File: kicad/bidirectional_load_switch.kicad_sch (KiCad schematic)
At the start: 10 parts, among them U1 SISS94DN-T1-GE3, U2 RTBS60M, U3 UCC23313DWYR, U4 DMN65D8L-7

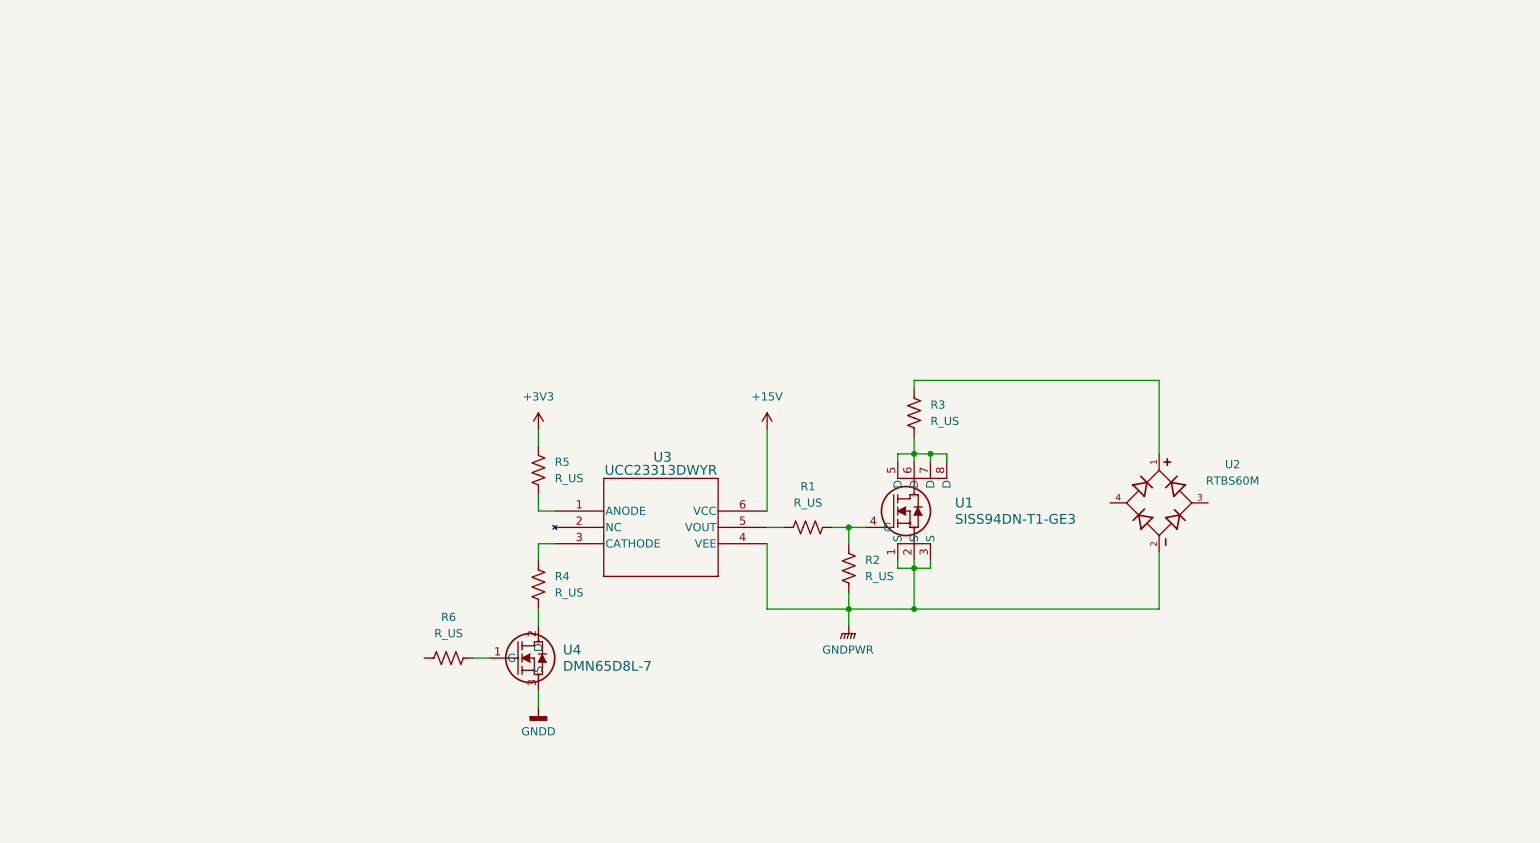
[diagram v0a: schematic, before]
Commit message: implementing switch design
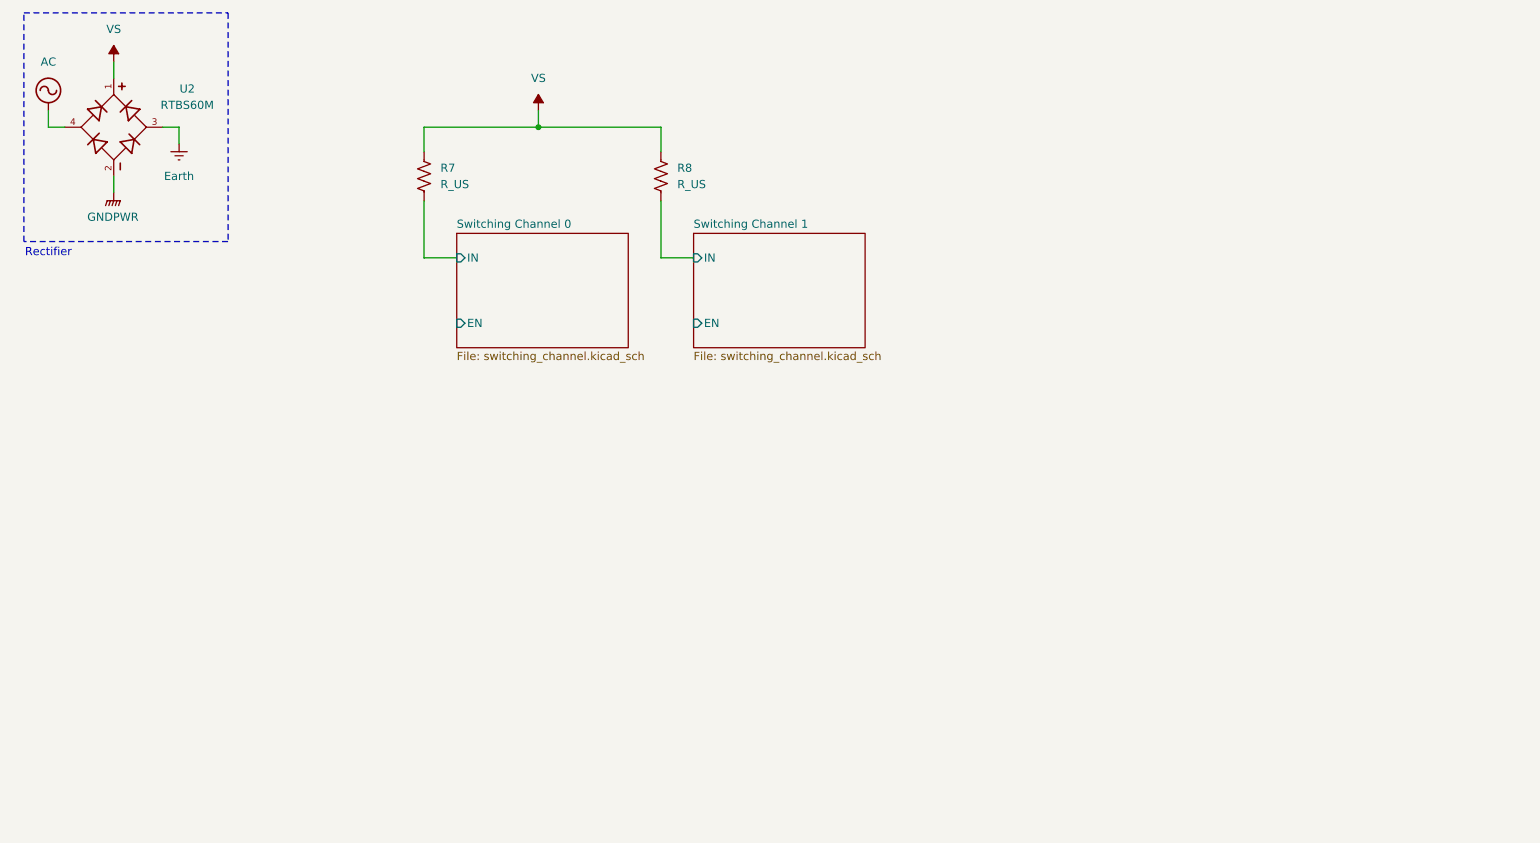
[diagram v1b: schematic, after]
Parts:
- removed R1, R2, R3, R4, R5, R6: R_US, Resistor_SMD:R_2512_6332Metric_Pad1.40x3.35mm_HandSolder, symbol Device:R_US
- removed U1: SISS94DN-T1-GE3, Big Mosfet:MOSFET_3DN-T1-GE3_VIS, symbol Mosfet:SISS94DN-T1-GE3
- removed U3: UCC23313DWYR, Gate Driver:SOIC6_DWY_TEX, symbol Gate Driver:UCC23313DWYR
- removed U4: DMN65D8L-7, Small Mosfet:SOT-23_2P9X1P3_DIO, symbol Small Mosfet:DMN65D8L-7
- added R7, R8: R_US, symbol Device:R_US
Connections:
- net VS: now reaches U2.1
- net VS: now also R7.1, R8.1
- net Earth: now reaches U2.3
- net AC: now reaches U2.4
- new net Switching Channel 0/IN: R7.2
- new net Switching Channel 1/IN: R8.2
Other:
- added sheet Switching Channel 0 (switching_channel.kicad_sch)
- added sheet Switching Channel 1 (switching_channel.kicad_sch)
- note added: "Rectifier"
- company: (none) -> University of Wisconsin-Platteville
- title: (none) -> Bidirectional Load Switch

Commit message: kicad
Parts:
- removed R7, R8: R_US, symbol Device:R_US
- added R25, R26, R27, R28, R29, R30, R31, R32: R_US, symbol Device:R_US
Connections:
- net Channel 0/IN: now also R25.2
- new net: R25.1, R26.1, R27.1, R28.1, R29.1, R30.1, R31.1, R32.1
- new net Channel 1/IN: R26.2
- new net Channel 2/IN: R27.2
- new net Channel 3/IN: R28.2
- new net Channel 4/IN: R29.2
- new net Channel 5/IN: R30.2
- new net Channel 6/IN: R31.2
- new net Channel 7/IN: R32.2
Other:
- sheet Switching Channel 0 renamed Channel 0
- removed sheet Switching Channel 1
- added sheet Channel 1 (switching_channel.kicad_sch)
- added sheet Channel 2 (switching_channel.kicad_sch)
- added sheet Channel 3 (switching_channel.kicad_sch)
- added sheet Channel 4 (switching_channel.kicad_sch)
- added sheet Channel 5 (switching_channel.kicad_sch)
- added sheet Channel 6 (switching_channel.kicad_sch)
- added sheet Channel 7 (switching_channel.kicad_sch)

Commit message: kicad
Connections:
- net VS: now also R25.1, R26.1, R27.1, R28.1, R29.1, R30.1, R31.1, R32.1
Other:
- moved on the sheet: R25, R26, R27, R28, R29, R30, R31, R32, U2

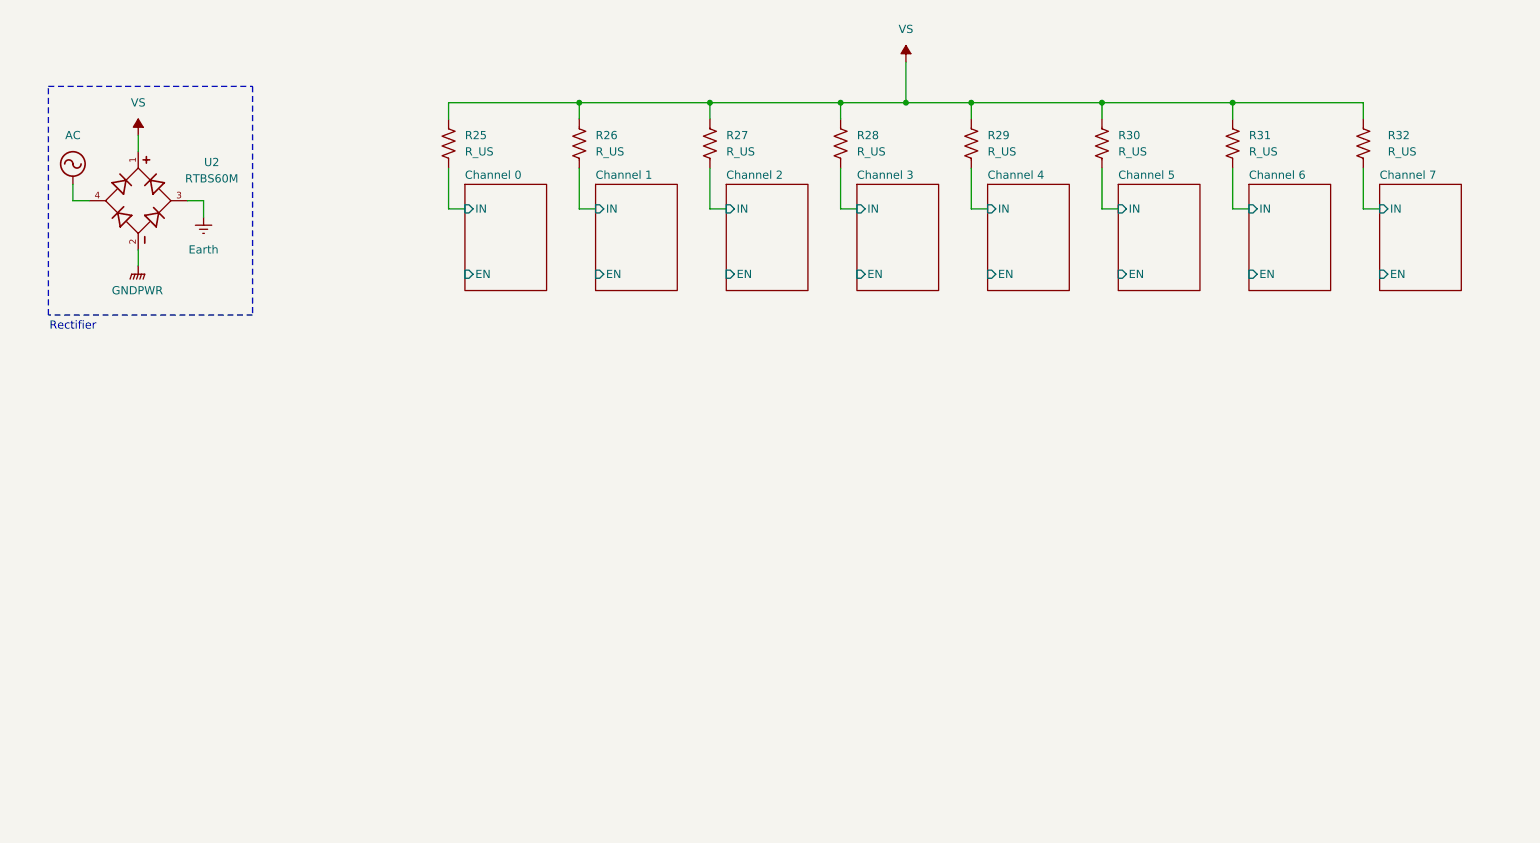
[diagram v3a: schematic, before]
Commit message: updated switch topology
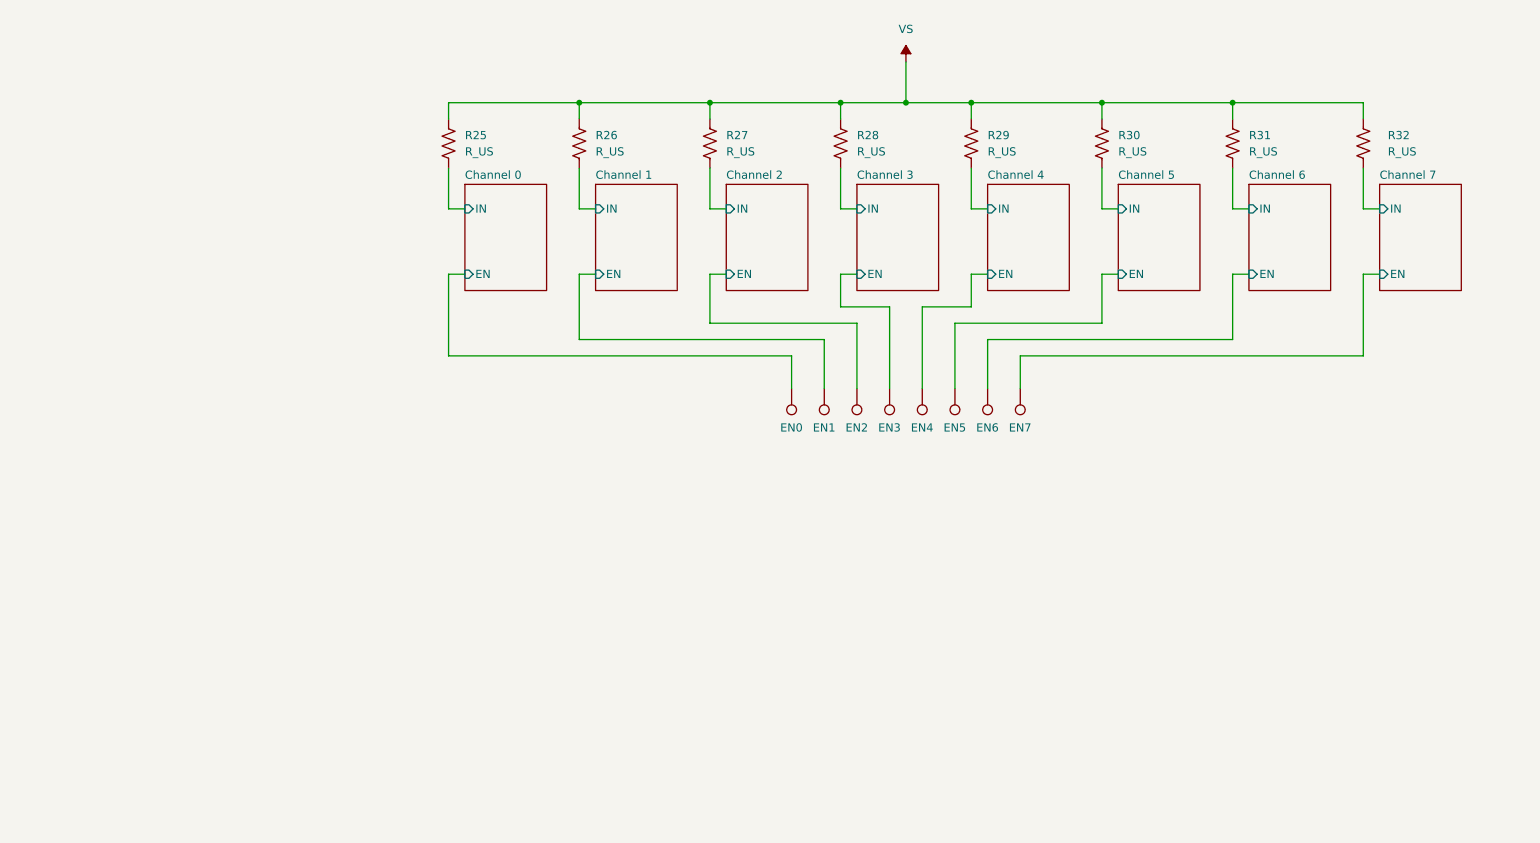
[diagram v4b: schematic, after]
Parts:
- removed U2: RTBS60M, Rectifier:SOIC500P990X195-4N, symbol Rectifier:RTBS60M
- added EN0, EN1, EN2, EN3, EN4, EN5, EN6, EN7: TestPoint, TestPoint:TestPoint_Pad_1.5x1.5mm, symbol Connector:TestPoint
- R25, R26, R27, R28, R29, R30, R31, R32: footprint (none) -> Resistor_SMD:R_1206_3216Metric_Pad1.30x1.75mm_HandSolder
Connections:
- net Channel 0/EN: now also EN0.1
- net Channel 1/EN: now also EN1.1
- net Channel 2/EN: now also EN2.1
- net Channel 3/EN: now also EN3.1
- net Channel 4/EN: now also EN4.1
- net Channel 5/EN: now also EN5.1
- net Channel 6/EN: now also EN6.1
- net Channel 7/EN: now also EN7.1
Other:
- note removed: "Rectifier"

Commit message: kicad
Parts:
- removed EN1, EN2, EN3, EN4, EN5, EN6, EN7: TestPoint, TestPoint:TestPoint_Pad_1.5x1.5mm, symbol Connector:TestPoint
- removed R26, R27, R28, R29, R30, R31, R32: R_US, Resistor_SMD:R_1206_3216Metric_Pad1.30x1.75mm_HandSolder, symbol Device:R_US
- renumbered R25 to RS1
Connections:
- net Channel 0/EN is gone; now on net Channel 1/EN: EN0.1
- net Channel 0/IN is gone; now on net Channel 1/IN: RS1.2
- net VS: no longer names the net of RS1.1
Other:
- removed sheet Channel 0
- removed sheet Channel 2
- removed sheet Channel 3
- removed sheet Channel 4
- removed sheet Channel 5
- removed sheet Channel 6
- removed sheet Channel 7
- added sheet Isolated DC-DC (isolated_dc_to_dc.kicad_sch)

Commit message: kicad
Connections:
- net Channel 1/EN renamed Channel 1/PWM
- net Channel 1/IN renamed Channel 1/RIN
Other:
- sheet Channel 1 ports: added PWM, RIN; removed EN, IN
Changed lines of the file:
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@@
 			)
 		)
-		(pin "IN" input
-			(at 85.09 45.72 180)
+		(pin "PWM" input
+			(at 85.09 55.88 180)
 			(effects
 				(font
@@
 			)
 		)
-		(pin "EN" input
-			(at 85.09 55.88 180)
+		(pin "RIN" input
+			(at 85.09 45.72 180)
 			(effects
 				(font

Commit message: kicad
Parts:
- added PWM2, PWM3, PWM4, PWM5, PWM6, PWM7, PWM8: TestPoint, TestPoint:TestPoint_Pad_1.5x1.5mm, symbol Connector:TestPoint
- added RS2, RS3, RS4, RS5, RS6, RS7, RS8: R_US, Resistor_SMD:R_1206_3216Metric_Pad1.30x1.75mm_HandSolder, symbol Device:R_US
- renumbered EN0 to PWM1
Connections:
- new net Channel 2/PWM: PWM2.1
- new net Channel 2/RIN: RS2.2
- new net Channel 3/PWM: PWM3.1
- new net Channel 3/RIN: RS3.2
- new net Channel 4/PWM: PWM4.1
- new net Channel 4/RIN: RS4.2
- new net Channel 5/RIN: RS5.2
- new net Channel 6/RIN: RS6.2
- new net Channel 7/RIN: RS7.2
- new net Channel 8/RIN: RS8.2
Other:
- added sheet Channel 2 (switching_channel.kicad_sch)
- added sheet Channel 3 (switching_channel.kicad_sch)
- added sheet Channel 4 (switching_channel.kicad_sch)
- added sheet Channel 5 (switching_channel.kicad_sch)
- added sheet Channel 6 (switching_channel.kicad_sch)
- added sheet Channel 7 (switching_channel.kicad_sch)
- added sheet Channel 8 (switching_channel.kicad_sch)
- moved on the sheet: PWM1

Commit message: kicad
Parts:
- removed PWM1, PWM2, PWM3, PWM4, PWM5, PWM6, PWM7, PWM8: TestPoint, TestPoint:TestPoint_Pad_1.5x1.5mm, symbol Connector:TestPoint
- added J101: Screw_Terminal_01x13, TerminalBlock:TerminalBlock_Xinya_XY308-2.54-13P_1x13_P2.54mm_Horizontal, symbol Connector:Screw_Terminal_01x13
- renumbered RS1 to RS101, RS2 to RS102, RS3 to RS103, RS4 to RS104, RS5 to RS105, RS6 to RS106, RS7 to RS107, RS8 to RS108
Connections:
- net AC_in: now reaches RS103.1
- net AC_in: now also RS101.1, RS102.1, RS104.1, RS105.1, RS106.1, RS107.1, RS108.1, J101.12 (Pin_12)
- new net 3v3: J101.2 (Pin_2)
- new net Earth: J101.13 (Pin_13)
- new net GND: J101.3 (Pin_3)
- new net PWM1: J101.4 (Pin_4)
- new net PWM2: J101.5 (Pin_5)
- new net PWM3: J101.6 (Pin_6)
- new net PWM4: J101.7 (Pin_7)
- new net PWM5: J101.8 (Pin_8)
- new net PWM6: J101.9 (Pin_9)
- new net PWM7: J101.10 (Pin_10)
- new net PWM8: J101.11 (Pin_11)
- new net VBAT_managed: J101.1 (Pin_1)
